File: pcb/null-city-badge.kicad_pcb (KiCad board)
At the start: 2 copper layers, 76.6 x 154.8 mm, 194 parts, among them J1 USB_C_Receptacle_USB2.0_16P, J10 Conn_01x10_Pin, J11 Conn_Coaxial_Small, J12 Conn_01x07_Pin, J2 Conn_01x02_Pin, J3 Conn_01x06_Pin, J4 Conn_01x24_Socket, J6 Conn_01x06_Pin, J8 Conn_01x06_Pin, Q1 SS8050, Q2 SS8050, Q3 IRLML0030, Q4 AO3401A, Q5 SS8050, U1 ESP32-S3-WROOM-1, U10 TCA9534, U13 CC1101RGP, U14 ME6211C33M5, U2 CP2102N-Axx-xQFN28, U3 SE050C2HQ1_Z01SDZ, U4 MCP73831-2-MC, U5 ME6211C33M5, U6 ME6211C33M5, U7 NS4168, Y2 26Mhz

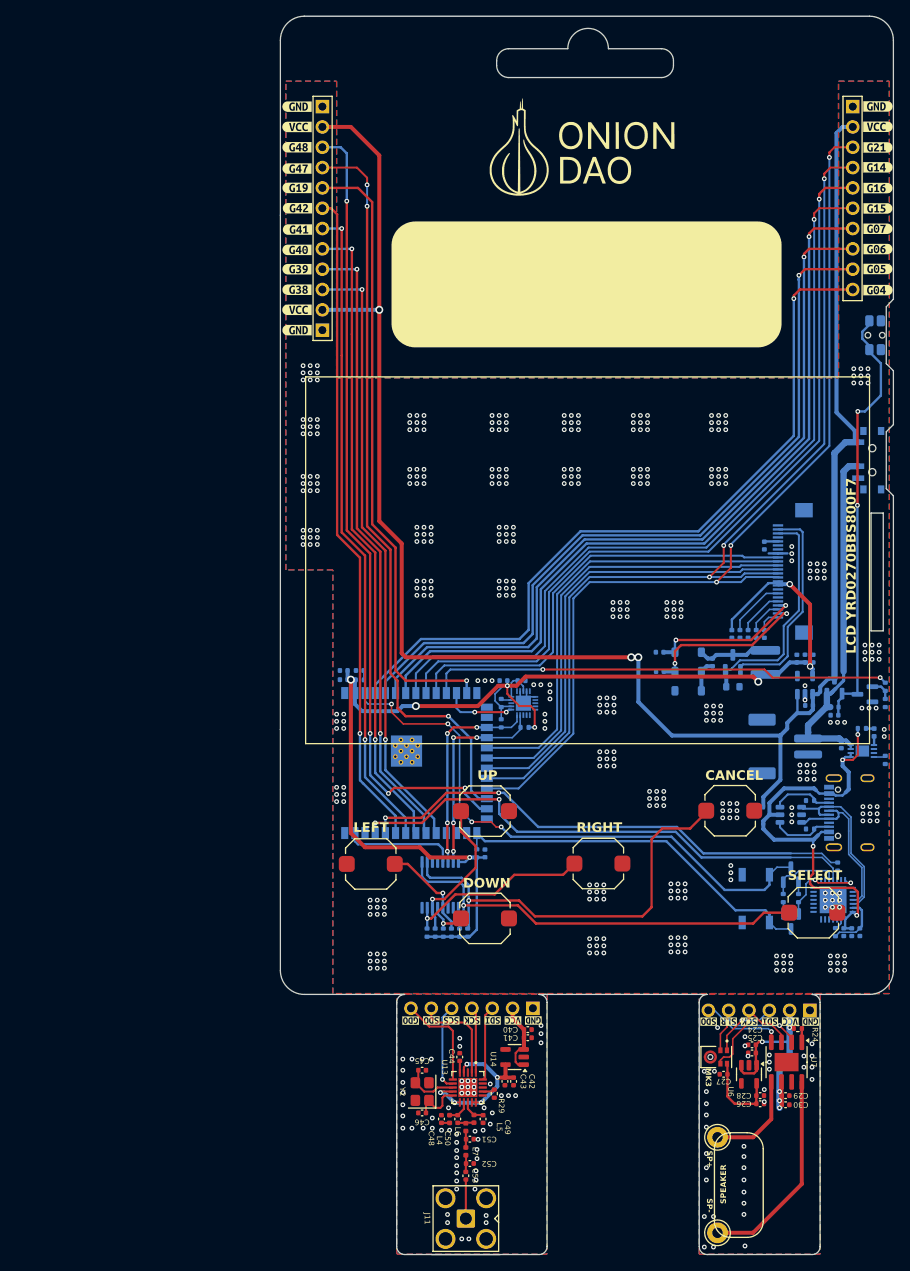
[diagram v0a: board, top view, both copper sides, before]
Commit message: feat: improve pinout and remove sdcard and lora module, update design
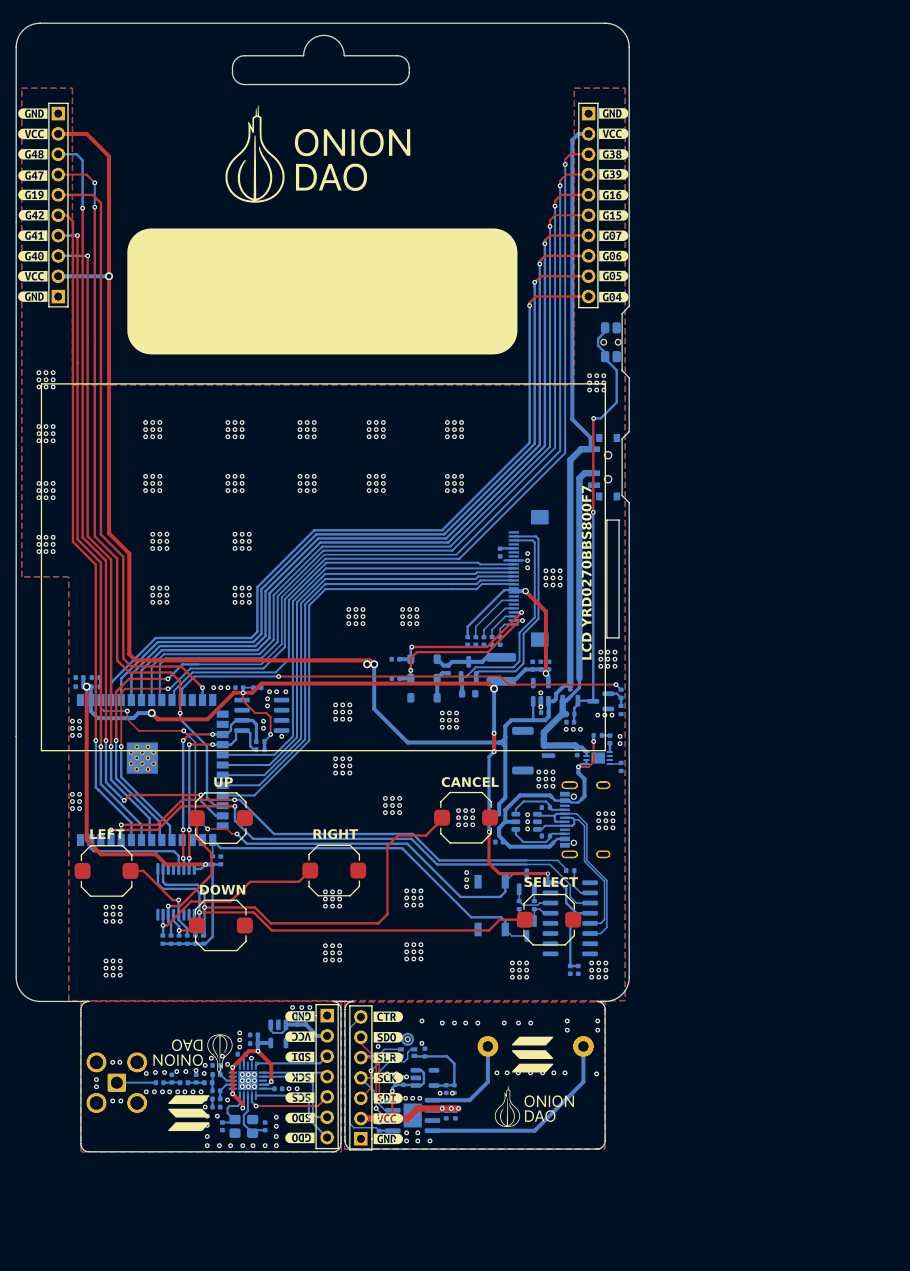
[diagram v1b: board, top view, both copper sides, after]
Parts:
- removed R19, R8: 10K, Resistor_SMD:R_0402_1005Metric
- removed U2: CP2102N-Axx-xQFN28, Package_DFN_QFN:QFN-28-1EP_5x5mm_P0.5mm_EP3.35x3.35mm
- removed U3: SE050C2HQ1_Z01SDZ, NIP_MOD:QFN40P300X300X33-21N
- removed kibuzzard-69D663D7: G***, kibuzzard-69D663D7
- removed kibuzzard-69D663E3: G***, kibuzzard-69D663E3
- removed kibuzzard-69D66608: G***, kibuzzard-69D66608
- removed kibuzzard-69D66615: G***, kibuzzard-69D66615
- removed kibuzzard-69D673D8: G***, kibuzzard-69D673D8
- removed kibuzzard-69D673DD: G***, kibuzzard-69D673DD
- removed kibuzzard-69D673E3: G***, kibuzzard-69D673E3
- removed kibuzzard-69D673EE: G***, kibuzzard-69D673EE
- removed kibuzzard-69D70141: G***, kibuzzard-69D70141
- removed kibuzzard-69D70146: G***, kibuzzard-69D70146
- removed kibuzzard-69D7014E: G***, kibuzzard-69D7014E
- removed kibuzzard-69D70154: G***, kibuzzard-69D70154
- added U15: CH340C, Package_SO:SOIC-16_3.9x9.9mm_P1.27mm, B.Cu at (106.2, 145.0)
- added U16: ATECC608B-SSHDA, Package_SO:SOIC-8_3.9x4.9mm_P1.27mm, B.Cu at (67.6, 119.6)
- added kibuzzard-69E6D5DE: G***, kibuzzard-69E6D5DE, F.Cu at (111.6, 52.0)
- added kibuzzard-69E6D5FA: G***, kibuzzard-69E6D5FA, F.Cu at (39.0, 62.3)
- added kibuzzard-69E6D601: G***, kibuzzard-69E6D601, F.Cu at (39.0, 59.7)
- added kibuzzard-69E6D610: G***, kibuzzard-69E6D610, F.Cu at (111.6, 49.5)
- added kibuzzard-69E6D61C: G***, kibuzzard-69E6D61C, B.Cu at (111.6, 49.5)
- added kibuzzard-69E6D626: G***, kibuzzard-69E6D626, B.Cu at (111.6, 52.0)
- added kibuzzard-69E6D63B: G***, kibuzzard-69E6D63B, B.Cu at (39.0, 62.2)
- added kibuzzard-69E6D641: G***, kibuzzard-69E6D641, B.Cu at (39.0, 59.7)
- added kibuzzard-69E6DA12: G***, kibuzzard-69E6DA12, F.Cu at (83.4, 157.3)
- added kibuzzard-69E6DA18: G***, kibuzzard-69E6DA18, B.Cu at (81.4, 157.4)
- C24, C25, C26, C27, C28, C29, C30, C40, C41, C42, C43, C44, C45, C46, C48, C49, C50, C51, C52, C53, J11, L4, L5, L6, L7, MK3, R24, R29, TP1, TP2, U13, U14, U6, U7, Y2, kibuzzard-69D7A5EF, kibuzzard-69D7A5F4 (x2), kibuzzard-69D7A626 (x2), kibuzzard-69D7A630 (x2), kibuzzard-69D7A638 (x2), kibuzzard-69D7A640 (x2), kibuzzard-69D7D86C, kibuzzard-69D7D873: moved to B.Cu
- G*** (x4), J12, kibuzzard-69D663C6 (x2), kibuzzard-69D70112 (x2), kibuzzard-69D7A260 (x2), kibuzzard-69D7A287 (x2), kibuzzard-69D7A28C (x2), kibuzzard-69D7A2FA, kibuzzard-69D7D7AD, kibuzzard-69D7D7BC: moved to F.Cu
- J2: footprint Connector_JST:JST_PH_S2B-PH-SM4-TB_1x02-1MP_P2.00mm_Horizontal -> Connector_JST:JST_GH_SM02B-GHS-TB_1x02-1MP_P1.25mm_Horizontal
- J3: value Conn_01x06_Pin -> Conn_01x04_Pin; footprint Connector_PinHeader_2.54mm:PinHeader_1x06_P2.54mm_Vertical -> Connector_PinHeader_2.54mm:PinHeader_1x04_P2.54mm_Vertical; moved to F.Cu
- J6: value Conn_01x06_Pin -> Conn_01x07_Pin; footprint Connector_PinHeader_2.54mm:PinHeader_1x06_P2.54mm_Vertical -> Connector_PinHeader_2.54mm:PinHeader_1x07_P2.54mm_Vertical; moved to F.Cu
- moved J6 58.4 mm to (80.0, 172.6), turned to 180 degrees
- moved kibuzzard-69D7A640 56.7 mm to (81.4, 172.7), turned to 90 degrees
- moved kibuzzard-69D663C6 54.2 mm to (83.4, 172.6), turned to 0 degrees
- moved R24 53.8 mm to (82.3, 171.1), turned to 90 degrees
- moved kibuzzard-69D7A638 53.7 mm to (81.4, 170.1), turned to 90 degrees
- moved kibuzzard-69D70112 51.2 mm to (83.4, 170.1), turned to 0 degrees
- moved kibuzzard-69D7A630 50.6 mm to (81.4, 167.6), turned to 90 degrees
- moved kibuzzard-69D7A28C 48.2 mm to (83.4, 167.5), turned to 0 degrees
- moved kibuzzard-69D7A626 47.7 mm to (81.4, 165.0), turned to 90 degrees
- moved U7 47.2 mm to (86.5, 169.7), turned to 0 degrees
- moved J11 46.8 mm to (49.5, 165.6), turned to -90 degrees
- moved C1 46.5 mm to (97.3, 135.5), turned to 180 degrees
- moved kibuzzard-69D7A287 45.3 mm to (83.4, 165.0), turned to 0 degrees
- moved C24 44.8 mm to (84.3, 165.4), turned to 90 degrees
- moved kibuzzard-69D7A5EF 44.8 mm to (81.4, 162.4), turned to 90 degrees
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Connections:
- C1 pad 1: Net-(U2-VDD) -> VBUS
- C2 pad 1: VBUS -> 3V3
- C3 pad 1: VBUS -> 3V3
- C9 pad 1: Net-(U3-VCC) -> 3V3
- J10 pad 3: /SDI -> /1SDI
- J10 pad 4: /SCK -> /1SCK
- J3 pad 3: /1SDI -> /1CS
- J3 pad 4: /1SCK -> /1SDO
- R24 pad 1: Net-(U7-CTRL) -> /SOUND MODULE/CTRL
- U7 pad 1: Net-(U7-CTRL) -> /SOUND MODULE/CTRL
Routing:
- net /SDI: track 120.1 -> 57.4 mm, vias 3 -> 0
- net /SCK: track 117.1 -> 56.9 mm, vias 3 -> 0
- net /1SDI: track 76.7 -> 132.3 mm, vias 2 -> 3
- net /1SCK: track 78.4 -> 129.9 mm, vias 2 -> 3
- net 3V3: track 158.1 -> 203.0 mm, vias 8 -> 12
- net /SOUND MODULE/CTRL: track 0.00 -> 19.8 mm
- net VBUS: track 56.1 -> 36.6 mm, vias 4 -> 2
- net /SE_EN: track 9.08 -> 0.00 mm, vias 2 -> 0
- net /DTR: track 11.2 -> 3.92 mm, vias 2 -> 0
- net Net-(U2-VDD): track 7.11 -> 0.00 mm
- net GND1: track 7.51 -> 2.35 mm, vias 393 -> 384
- net Net-(U3-VCC): track 4.27 -> 0.00 mm
- net /D-: track 21.3 -> 25.2 mm
- net /TX0: track 65.6 -> 69.1 mm
- net /RTS: track 9.09 -> 5.72 mm
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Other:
- board size 76.6 x 154.8 mm -> 76.6 x 141.1 mm

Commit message: fix sub ghz, epaper and audio module
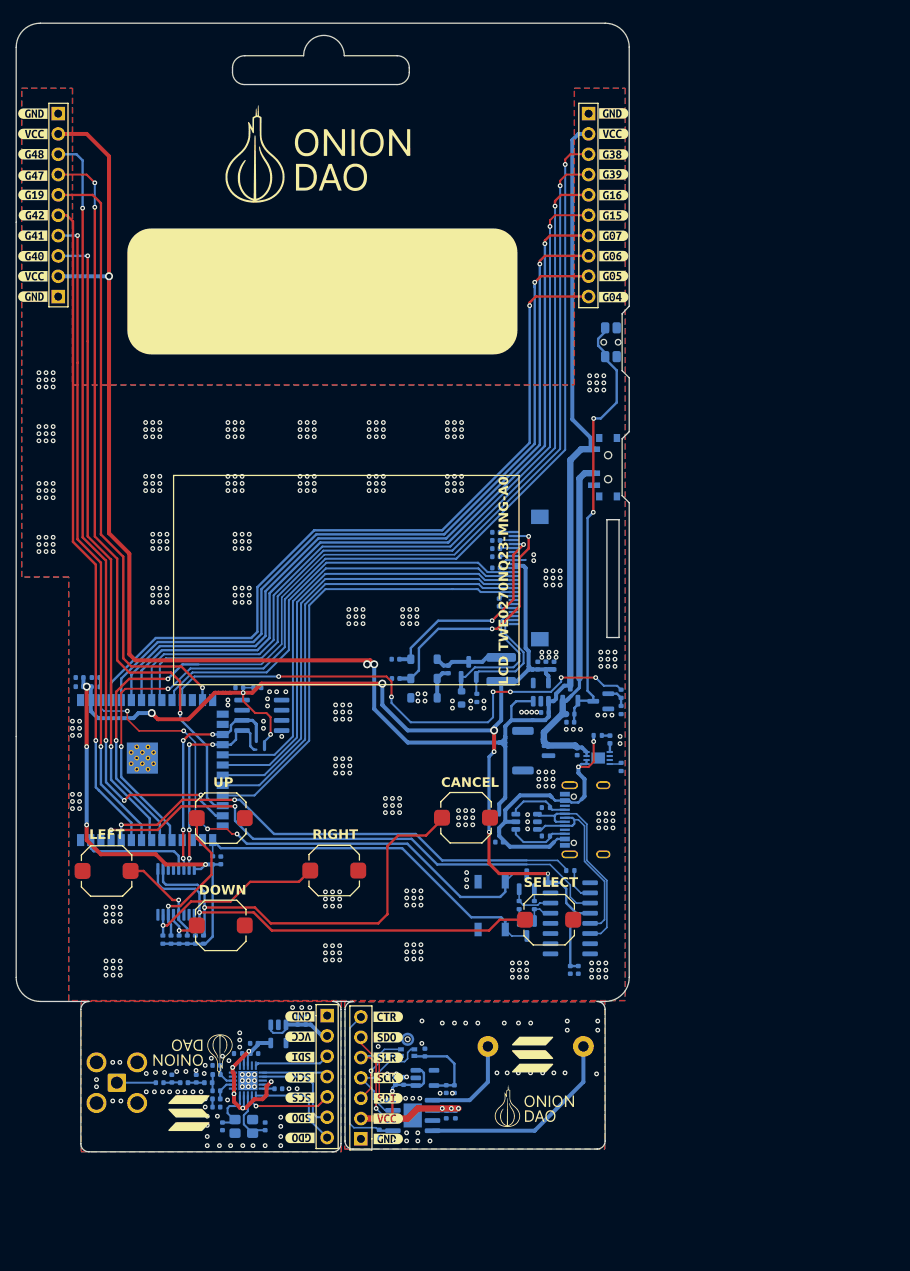
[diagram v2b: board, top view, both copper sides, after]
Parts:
- removed R11, R12: 2K2, Resistor_SMD:R_0402_1005Metric
- added R8: 56K, Resistor_SMD:R_0402_1005Metric, B.Cu at (94.5, 117.5)
- moved C15 13.6 mm to (96.9, 96.8), turned to 0 degrees
- moved C16 12.6 mm to (96.9, 97.8), turned to 0 degrees
- moved C17 11.6 mm to (96.9, 98.8), turned to 0 degrees
- moved C18 10.8 mm to (96.9, 99.8), turned to 0 degrees
- moved C14 9.80 mm to (96.9, 101.2), turned to 0 degrees
- moved C19 6.24 mm to (97.3, 105.5), turned to -90 degrees
- moved C43 1.25 mm to (66.7, 161.9), turned to 0 degrees
- moved C42 1.06 mm to (66.6, 160.7)
- moved R20 1.03 mm to (92.6, 117.5), turned to 90 degrees
- moved R24 0.88 mm to (82.3, 172.0), turned to -90 degrees
- moved C10 0.64 mm to (102.1, 113.4)
- moved C5 0.64 mm to (104.1, 113.4)
- moved C6 0.63 mm to (103.1, 113.4)
- moved R29 0.47 mm to (64.6, 161.9)
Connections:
- C15 pad 2: Net-(J4-Pin_24) -> Net-(J4-Pin_1)
- C16 pad 2: Net-(J4-Pin_22) -> Net-(J4-Pin_3)
- C17 pad 2: Net-(J4-Pin_20) -> Net-(J4-Pin_5)
- C18 pad 2: Net-(J4-Pin_18) -> Net-(J4-Pin_7)
- C19 pad 2: Net-(J4-Pin_5) -> Net-(J4-Pin_20)
- J4 pad 1: unconnected-(J4-Pin_1-Pad1) -> Net-(J4-Pin_1)
- J4 pad 10: /RS -> 3V3
- J4 pad 11: /DC -> /SDI
- J4 pad 12: /CS -> /SCK
- J4 pad 13: /SCK -> /CS
- J4 pad 14: /SDI -> /DC
- J4 pad 15: 3V3 -> /RS
- J4 pad 16: 3V3 -> /BUSY
- J4 pad 17: unconnected-(J4-Pin_17-Pad17) -> GND1
- J4 pad 18: Net-(J4-Pin_18) -> unconnected-(J4-Pin_18-Pad18)
- J4 pad 2: /GDR -> /VGL
- J4 pad 21: /VGH -> unconnected-(J4-Pin_21-Pad21)
- J4 pad 22: Net-(J4-Pin_22) -> /RESE
- J4 pad 23: /VGL -> /GDR
- J4 pad 24: Net-(J4-Pin_24) -> unconnected-(J4-Pin_24-Pad24)
- J4 pad 3: /RESE -> Net-(J4-Pin_3)
- J4 pad 4: unconnected-(J4-Pin_4-Pad4) -> /VGH
- J4 pad 7: unconnected-(J4-Pin_7-Pad7) -> Net-(J4-Pin_7)
- J4 pad 9: /BUSY -> 3V3
- R24 pad 2: VSYS_1 -> GND_1
- U1 pad 10: /BUSY -> /SDI
- U1 pad 19: /RS -> /SCK
- U1 pad 20: /DC -> /CS
- U1 pad 21: /CS -> /DC
- U1 pad 22: /SCK -> /RS
- U1 pad 23: /SDI -> /BUSY
- U13 pad 18: GND_4 -> 3V3_4
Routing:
- net /RESE: track 28.5 -> 17.8 mm
- net /VGL: track 20.9 -> 31.4 mm
- net /GDR: track 26.3 -> 16.3 mm
- net /PWR: track 57.6 -> 66.0 mm, vias 2 -> 6
- net Net-(J4-Pin_18): track 7.41 -> 0.00 mm
- net /VGH: track 19.4 -> 26.8 mm
- net Net-(J4-Pin_22): track 4.33 -> 0.00 mm
- net Net-(J4-Pin_20): track 5.76 -> 1.92 mm
- net Net-(J4-Pin_24): track 2.97 -> 0.00 mm
- net /SDI: track 57.4 -> 54.5 mm
- net /BUSY: track 54.8 -> 57.1 mm
- net VSYS: track 234.4 -> 236.7 mm
- net 3V3: track 203.0 -> 205.2 mm
- net GND1: track 2.35 -> 4.56 mm, vias 384 -> 391
- net Net-(J4-Pin_7): track 0.00 -> 1.77 mm
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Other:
- board text added: "LCD TWE0270NQ23-MNG-A0"
- board text removed: "LCD YRD0270BBS800F7"
